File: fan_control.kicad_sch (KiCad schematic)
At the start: 1 part, among them J1 Conn_01x04

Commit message: do some pcb routing
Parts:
- renumbered J1 to J2
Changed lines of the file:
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@@
 		(dnp no)
 		(fields_autoplaced yes)
-		(property "Reference" "#PWR01"
+		(property "Reference" "#PWR022"
 			(at 144.78 118.11 0)
 			(hide yes)
@@
 			(project "gse_control_node"
 				(path "/24817451-dfe0-4b9a-9d93-7304529c9d58/3178ca55-81b8-4bea-837c-8a6c63e16663"
-					(reference "#PWR019")
+					(reference "#PWR069")
 					(unit 1)
 				)
 				(path "/24817451-dfe0-4b9a-9d93-7304529c9d58/9cf28330-c8ca-424a-aab2-bcebd5b04616"
-					(reference "#PWR01")
+					(reference "#PWR022")
 					(unit 1)
 				)
@@
 		(dnp no)
 		(fields_autoplaced yes)
-		(property "Reference" "#PWR02"
+		(property "Reference" "#PWR023"
 			(at 158.75 110.49 0)
 			(hide yes)
@@
 			(project "gse_control_node"
 				(path "/24817451-dfe0-4b9a-9d93-7304529c9d58/3178ca55-81b8-4bea-837c-8a6c63e16663"
-					(reference "#PWR021")
+					(reference "#PWR070")
 					(unit 1)
 				)
 				(path "/24817451-dfe0-4b9a-9d93-7304529c9d58/9cf28330-c8ca-424a-aab2-bcebd5b04616"
-					(reference "#PWR02")
+					(reference "#PWR023")
 					(unit 1)
 				)
@@
 		(dnp no)
 		(fields_autoplaced yes)
-		(property "Reference" "J1"
+		(property "Reference" "J2"
 			(at 138.43 96.52 0)
 			(show_name no)
@@
 			(project "gse_control_node"
 				(path "/24817451-dfe0-4b9a-9d93-7304529c9d58/3178ca55-81b8-4bea-837c-8a6c63e16663"
-					(reference "J8")
+					(reference "J6")
 					(unit 1)
 				)
 				(path "/24817451-dfe0-4b9a-9d93-7304529c9d58/9cf28330-c8ca-424a-aab2-bcebd5b04616"
-					(reference "J1")
-					(unit 1)
-				)
+					(reference "J2")
+					(unit 1)
+				)

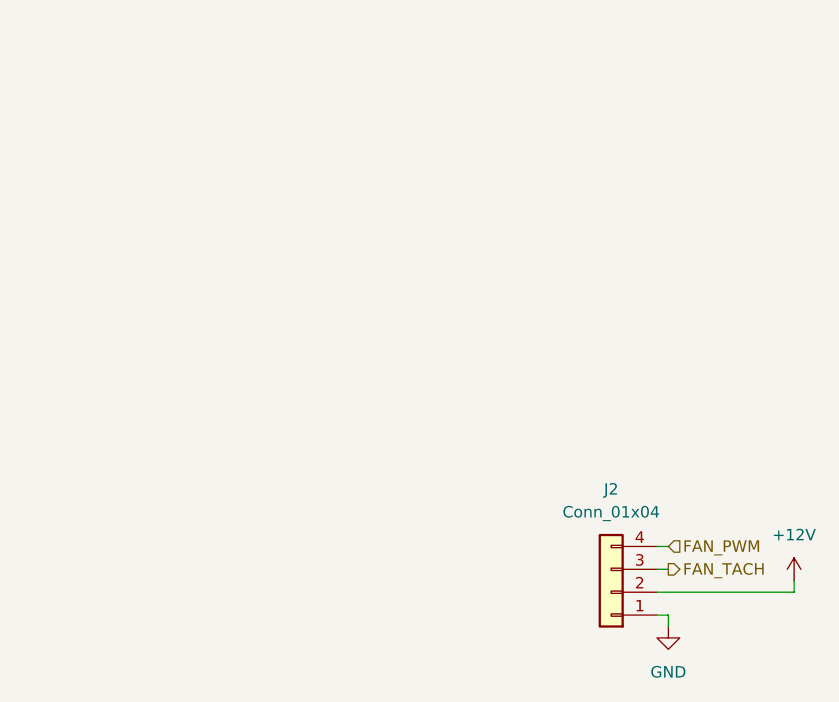
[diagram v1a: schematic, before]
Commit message: remove unneccesary component fields
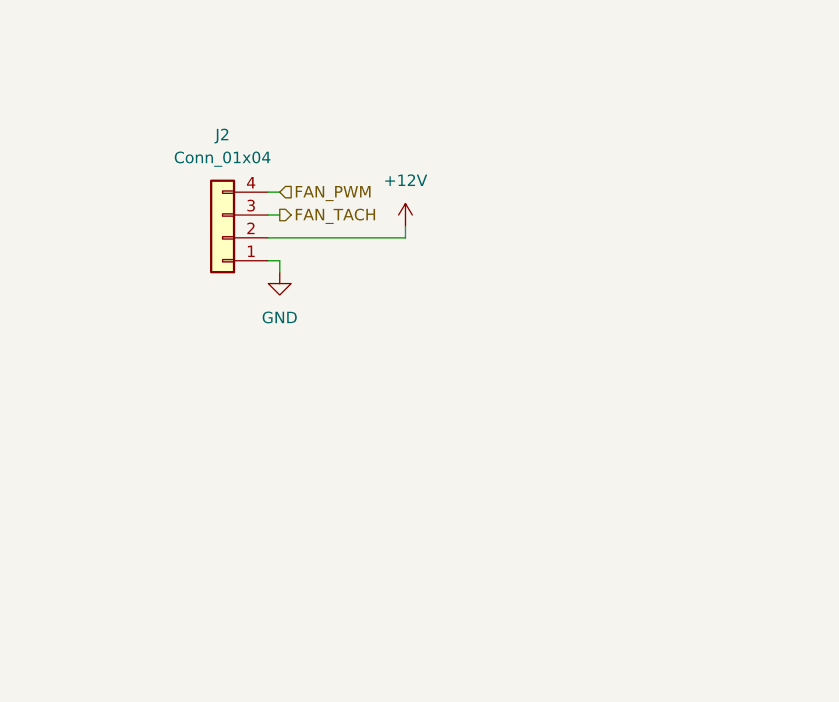
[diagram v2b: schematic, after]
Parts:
- J2: LCSC (none) -> N/A; now left out of the parts list
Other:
- moved on the sheet: J2
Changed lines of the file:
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@@
 	(generator "eeschema")
 	(generator_version "10.0")
-	(paper "A4")
-	(wire
-		(pts
-			(xy 143.51 105.41) (xy 144.78 105.41)
-		)
-		(stroke
-			(width 0)
-			(type default)
-		)
-	)
-	(wire
-		(pts
-			(xy 158.75 107.95) (xy 158.75 106.68)
-		)
-		(stroke
-			(width 0)
-			(type default)
-		)
-	)
-	(wire
-		(pts
-			(xy 143.51 107.95) (xy 158.75 107.95)
-		)
-		(stroke
-			(width 0)
-			(type default)
-		)
-	)
-	(wire
-		(pts
-			(xy 143.51 102.87) (xy 144.78 102.87)
-		)
-		(stroke
-			(width 0)
-			(type default)
-		)
-	)
-	(wire
-		(pts
-			(xy 143.51 110.49) (xy 144.78 110.49)
-		)
-		(stroke
-			(width 0)
-			(type default)
-		)
-	)
-	(wire
-		(pts
-			(xy 144.78 110.49) (xy 144.78 111.76)
+	(paper "A5")
+	(wire
+		(pts
+			(xy 100.33 66.04) (xy 101.6 66.04)
+		)
+		(stroke
+			(width 0)
+			(type default)
+		)
+	)
+	(wire
+		(pts
+			(xy 115.57 68.58) (xy 115.57 67.31)
+		)
+		(stroke
+			(width 0)
+			(type default)
+		)
+	)
+	(wire
+		(pts
+			(xy 100.33 68.58) (xy 115.57 68.58)
+		)
+		(stroke
+			(width 0)
+			(type default)
+		)
+	)
+	(wire
+		(pts
+			(xy 100.33 63.5) (xy 101.6 63.5)
+		)
+		(stroke
+			(width 0)
+			(type default)
+		)
+	)
+	(wire
+		(pts
+			(xy 100.33 71.12) (xy 101.6 71.12)
+		)
+		(stroke
+			(width 0)
+			(type default)
+		)
+	)
+	(wire
+		(pts
+			(xy 101.6 71.12) (xy 101.6 72.39)
 		)
 		(stroke
@@
 	(hierarchical_label "FAN_PWM"
 		(shape input)
-		(at 144.78 102.87 0)
+		(at 101.6 63.5 0)
 		(effects
 			(font
@@
 	(hierarchical_label "FAN_TACH"
 		(shape output)
-		(at 144.78 105.41 0)
+		(at 101.6 66.04 0)
 		(effects
 			(font
@@
 	(symbol
 		(lib_id "power:GND")
-		(at 144.78 111.76 0)
+		(at 101.6 72.39 0)
 		(unit 1)
 		(body_style 1)
@@
 		(fields_autoplaced yes)
 		(property "Reference" "#PWR022"
-			(at 144.78 118.11 0)
+			(at 101.6 78.74 0)
 			(hide yes)
 			(show_name no)
@@
 		)
 		(property "Value" "GND"
-			(at 144.78 116.84 0)
+			(at 101.6 77.47 0)
 			(show_name no)
 			(do_not_autoplace no)
@@
 		)
 		(property "Footprint" ""
-			(at 144.78 111.76 0)
+			(at 101.6 72.39 0)
 			(hide yes)
 			(show_name no)
@@
 		)
 		(property "Datasheet" ""
-			(at 144.78 111.76 0)
+			(at 101.6 72.39 0)
 			(hide yes)
 			(show_name no)
@@
 		)
 		(property "Description" "Power symbol creates a global label with name \"GND\" , ground"
-			(at 144.78 111.76 0)
+			(at 101.6 72.39 0)
 			(hide yes)
 			(show_name no)
@@
 	(symbol
 		(lib_id "power:+12V")
-		(at 158.75 106.68 0)
+		(at 115.57 67.31 0)
 		(unit 1)
 		(body_style 1)
@@
 		(fields_autoplaced yes)
 		(property "Reference" "#PWR023"
-			(at 158.75 110.49 0)
+			(at 115.57 71.12 0)
 			(hide yes)
 			(show_name no)
@@
 		)
 		(property "Value" "+12V"
-			(at 158.75 101.6 0)
+			(at 115.57 62.23 0)
 			(show_name no)
 			(do_not_autoplace no)
@@
 		)
 		(property "Footprint" ""
-			(at 158.75 106.68 0)
+			(at 115.57 67.31 0)
 			(hide yes)
 			(show_name no)
@@
 		)
 		(property "Datasheet" ""
-			(at 158.75 106.68 0)
+			(at 115.57 67.31 0)
 			(hide yes)
 			(show_name no)
@@
 		)
 		(property "Description" "Power symbol creates a global label with name \"+12V\""
-			(at 158.75 106.68 0)
+			(at 115.57 67.31 0)
 			(hide yes)
 			(show_name no)
@@
 	(symbol
 		(lib_id "Connector_Generic:Conn_01x04")
-		(at 138.43 107.95 180)
+		(at 95.25 68.58 180)
 		(unit 1)
 		(body_style 1)
 		(exclude_from_sim no)
-		(in_bom yes)
+		(in_bom no)
 		(on_board yes)
-		(in_pos_files yes)
+		(in_pos_files no)
 		(dnp no)
 		(fields_autoplaced yes)
 		(property "Reference" "J2"
-			(at 138.43 96.52 0)
+			(at 95.25 57.15 0)
 			(show_name no)
 			(do_not_autoplace no)
@@
 		)
 		(property "Value" "Conn_01x04"
-			(at 138.43 99.06 0)
+			(at 95.25 59.69 0)
 			(show_name no)
 			(do_not_autoplace no)
@@
 		)
 		(property "Footprint" "Connector_Molex:Molex_KK-254_AE-6410-04A_1x04_P2.54mm_Vertical"
-			(at 138.43 107.95 0)
+			(at 95.25 68.58 0)
 			(hide yes)
 			(show_name no)
@@
 		)
 		(property "Datasheet" ""
-			(at 138.43 107.95 0)
+			(at 95.25 68.58 0)
 			(hide yes)
 			(show_name no)
@@
 		)
 		(property "Description" "Generic connector, single row, 01x04, script generated (kicad-library-utils/schlib/autogen/connector/)"
-			(at 138.43 107.95 0)
-			(hide yes)
-			(show_name no)
+			(at 95.25 68.58 0)
+			(hide yes)
+			(show_name no)
+			(do_not_autoplace no)
+			(effects
+				(font
+					(size 1.27 1.27)
+				)
+			)
+		)
+		(property "LCSC" "N/A"
+			(at 95.25 68.58 0)
+			(hide yes)
+			(show_name no)

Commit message: add tachometer pullup and pwm low side fet for fans
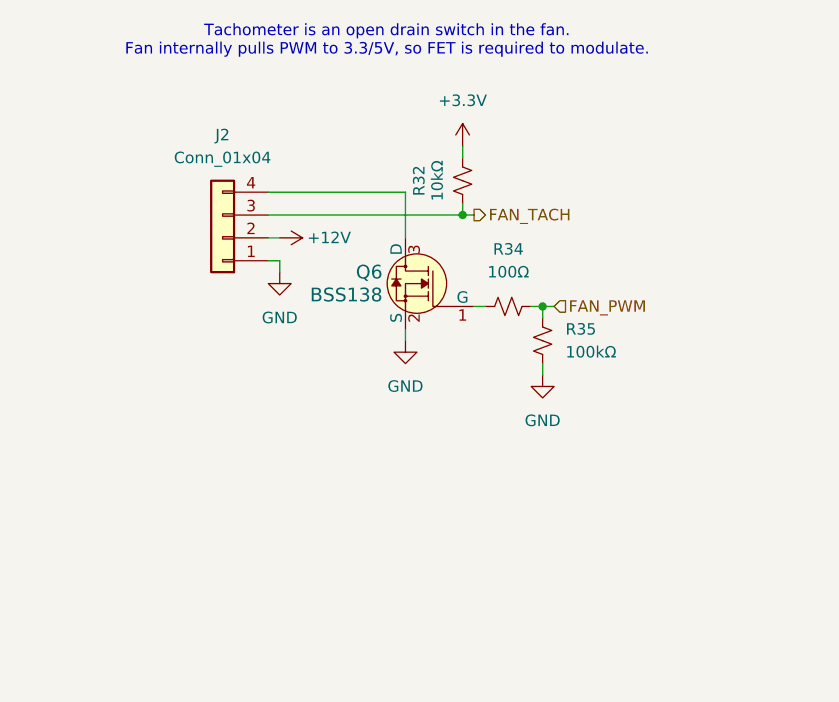
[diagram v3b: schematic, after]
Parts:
- added Q6: BSS138, Package_TO_SOT_SMD:SOT-23-3, symbol dk_Transistors-FETs-MOSFETs-Single:BSS138
- added R32: 10kΩ, Resistor_SMD:R_0603_1608Metric, symbol Device:R_Small_US
- added R34: 100Ω, Resistor_SMD:R_0603_1608Metric, symbol Device:R_Small_US
- added R35: 100kΩ, Resistor_SMD:R_0603_1608Metric, symbol Device:R_Small_US
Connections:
- net FAN_PWM: now also R34.2, R35.1; no longer J2.4 (Pin_4)
- net FAN_TACH: now also R32.1
- net GND: now also Q6.2 (S), R35.2
- new net: Q6.1 (G), R34.1
- new net: J2.4 (Pin_4), Q6.3 (D)
- new net +3.3V: R32.2
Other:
- note added: "Tachometer is an open drain switch in the fan. Fan internally pulls PWM to 3.3/5V, so FET is required to modulate."

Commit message: add back bss138 to jlcpcb bom
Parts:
- Q6: now in the parts list
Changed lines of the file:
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@@
 		(body_style 1)
 		(exclude_from_sim no)
-		(in_bom no)
+		(in_bom yes)
 		(on_board yes)
-		(in_pos_files no)
+		(in_pos_files yes)
 		(dnp no)
 		(property "Reference" "Q6"
